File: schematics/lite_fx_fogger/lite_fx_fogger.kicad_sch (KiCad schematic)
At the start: 13 parts

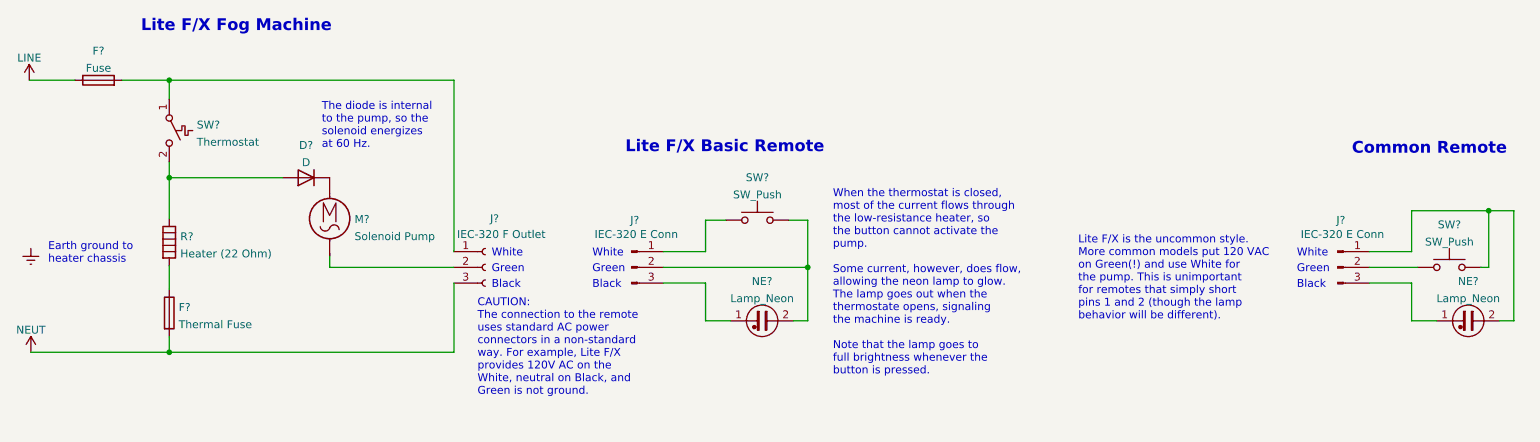
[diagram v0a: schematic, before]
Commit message: Triple checking how the basic wired remotes work with fog machines.
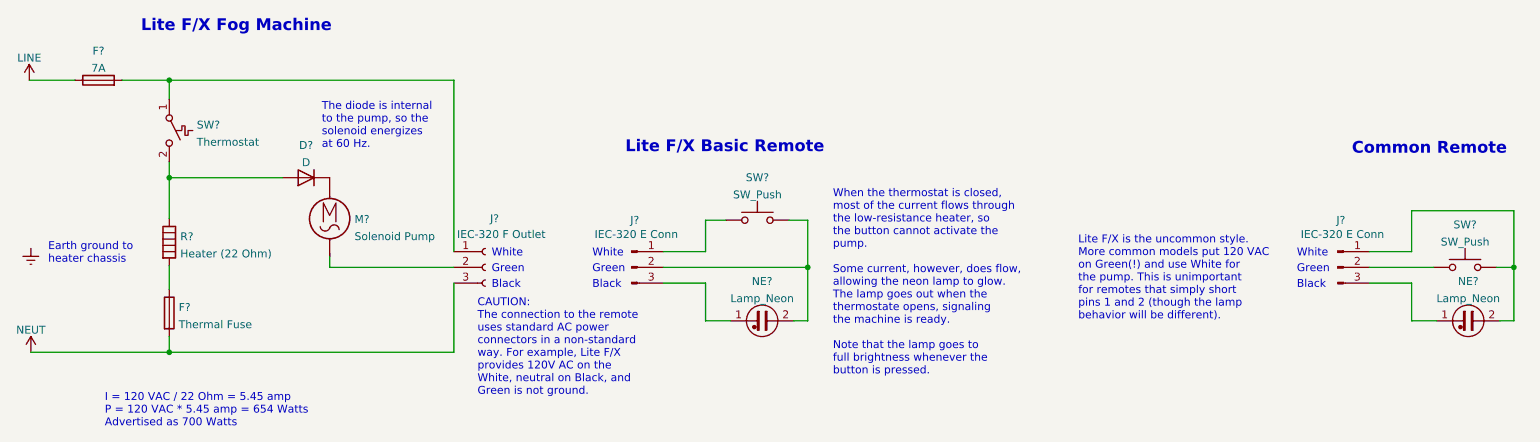
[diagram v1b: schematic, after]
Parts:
- F?: value Fuse -> 7A
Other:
- note added: "I = 120 VAC / 22 Ohm = 5.45 amp P = 120 VAC * 5.45 amp = 654 Watts Advertised as 700 Watts"
- title: Lite F/X Fog Machine -> Lite F/X 1741 Fog Machine
- moved on the sheet: SW?
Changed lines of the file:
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@@
   (paper "USLetter")
   (title_block
-    (title "Lite F/X Fog Machine")
-    (comment 1 "To illustrate how different remotes work.")
+    (title "Lite F/X 1741 Fog Machine")
+    (comment 1 "For reference only.")
+    (comment 2 "Representative of a less common \"party-store\" consumer fog machine.")
+  )
+  (junction (at 260.096 94.234) (diameter 0) (color 0 0 0 0)
   )
   (junction (at 42.926 79.756) (diameter 0) (color 0 0 0 0)
@@
   (junction (at 42.926 64.008) (diameter 0) (color 0 0 0 0)
   )
-  (junction (at 256.032 85.09) (diameter 0) (color 0 0 0 0)
-  )
   (wire (pts (xy 129.54 102.87) (xy 133.604 102.87))
     (stroke (width 0) (type default) (color 0 0 0 0))
@@
     (stroke (width 0) (type default) (color 0 0 0 0))
   )
-  (wire (pts (xy 243.586 85.09) (xy 256.032 85.09))
-    (stroke (width 0) (type default) (color 0 0 0 0))
-  )
   (wire (pts (xy 143.002 86.614) (xy 146.05 86.614))
     (stroke (width 0) (type default) (color 0 0 0 0))
@@
     (stroke (width 0) (type default) (color 0 0 0 0))
   )
-  (wire (pts (xy 260.096 85.09) (xy 260.096 102.87))
+  (wire (pts (xy 260.096 85.09) (xy 260.096 94.234))
     (stroke (width 0) (type default) (color 0 0 0 0))
   )
@@
     (stroke (width 0) (type default) (color 0 0 0 0))
   )
-  (wire (pts (xy 260.096 85.09) (xy 256.032 85.09))
+  (wire (pts (xy 243.586 85.09) (xy 260.096 85.09))
     (stroke (width 0) (type default) (color 0 0 0 0))
   )
@@
     (stroke (width 0) (type default) (color 0 0 0 0))
   )
-  (wire (pts (xy 236.728 94.234) (xy 244.602 94.234))
+  (wire (pts (xy 236.728 94.234) (xy 247.142 94.234))
     (stroke (width 0) (type default) (color 0 0 0 0))
   )
@@
     (stroke (width 0) (type default) (color 0 0 0 0))
   )
+  (wire (pts (xy 257.302 94.234) (xy 260.096 94.234))
+    (stroke (width 0) (type default) (color 0 0 0 0))
+  )
   (wire (pts (xy 122.682 94.234) (xy 146.05 94.234))
     (stroke (width 0) (type default) (color 0 0 0 0))
@@
     (stroke (width 0) (type default) (color 0 0 0 0))
   )
-  (wire (pts (xy 256.032 94.234) (xy 254.762 94.234))
-    (stroke (width 0) (type default) (color 0 0 0 0))
-  )
   (wire (pts (xy 243.586 85.09) (xy 243.586 91.694))
     (stroke (width 0) (type default) (color 0 0 0 0))
@@
     (stroke (width 0) (type default) (color 0 0 0 0))
   )
-  (wire (pts (xy 256.032 85.09) (xy 256.032 94.234))
+  (wire (pts (xy 260.096 94.234) (xy 260.096 102.87))
     (stroke (width 0) (type default) (color 0 0 0 0))
   )
@@
     (effects (font (size 1.27 1.27)) (justify left bottom))
   )
+  (text "I = 120 VAC / 22 Ohm = 5.45 amp\nP = 120 VAC * 5.45 amp = 654 Watts\nAdvertised as 700 Watts"
+    (at 32.512 120.142 0)
+    (effects (font (size 1.27 1.27)) (justify left bottom))
+  )
   (text "White" (at 94.996 92.71 0)
     (effects (font (size 1.27 1.27)) (justify left bottom))
@@
     (in_bom yes) (on_board yes) (fields_autoplaced)
     (property "Reference" "F?" (id 0) (at 31.496 59.2795 90))
-    (property "Value" "Fuse" (id 1) (at 31.496 62.0546 90))
+    (property "Value" "7A" (id 1) (at 31.496 62.0546 90))
     (property "Footprint" "" (id 2) (at 31.496 65.786 90)
       (effects (font (size 1.27 1.27)) hide)
@@
     (pin "2")
   )
-  (symbol (lib_id "Switch:SW_Push") (at 249.682 94.234 0) (unit 1)
+  (symbol (lib_id "Switch:SW_Push") (at 252.222 94.234 0) (unit 1)
     (in_bom yes) (on_board yes)
-    (property "Reference" "SW?" (id 0) (at 249.682 87.3465 0))
-    (property "Value" "SW_Push" (id 1) (at 249.682 90.1216 0))
-    (property "Footprint" "" (id 2) (at 249.682 89.154 0)
-      (effects (font (size 1.27 1.27)) hide)
-    )
-    (property "Datasheet" "~" (id 3) (at 249.682 89.154 0)
+    (property "Reference" "SW?" (id 0) (at 252.222 87.3465 0))
+    (property "Value" "SW_Push" (id 1) (at 252.222 90.1216 0))
+    (property "Footprint" "" (id 2) (at 252.222 89.154 0)
+      (effects (font (size 1.27 1.27)) hide)
+    )
+    (property "Datasheet" "~" (id 3) (at 252.222 89.154 0)
       (effects (font (size 1.27 1.27)) hide)
     )
@@
     )
     (path "/0e8f7fc0-2ef2-4b90-9c15-8a3a601ee459"
-      (reference "F?") (unit 1) (value "Fuse") (footprint "")
+      (reference "F?") (unit 1) (value "7A") (footprint "")
     )
     (path "/4a6f7f58-ffa1-4ce0-84a4-a43028bdaf25"
